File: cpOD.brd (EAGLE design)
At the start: 49.5 x 27.9 mm, 29 parts, among them IC1 LM358D, Q1 2N7002

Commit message: 2.0B-WIP
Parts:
- added R11: 10K, SPCoast:PT-10S
- added R12: 10K, SPCoast:TC33X
- C2: value 1uF -> 1.0uF
- R1: value 2.2M -> 2M2
- R10: value 10k -> 3K3
- R2, R3, R6: value 10k -> 10K
- R7: value 3.3k -> 1M
- R8: value 1M -> 10K; device SPCoast:0603-RES -> SPCoast:ST-4
- R9: value 10k -> 10K; device SPCoast:TC33X -> SPCoast:0603-RES
- moved R8 8.75 mm to (43.4, 17.1), turned to 90 degrees
- moved R9 8.64 mm to (45.7, 13.3), turned to 180 degrees
- moved LED1 6.11 mm to (46.6, 7.87), turned to 90 degrees
- moved R10 4.58 mm to (45.7, 11.4)
- moved R7 2.03 mm to (35.6, 13.3)
- moved C1 1.90 mm to (15.2, 11.4)
- moved FID2 0.90 mm to (47.6, 1.91)
- moved FID1 0.64 mm to (1.91, 25.4)
- turned R4 to 0 degrees
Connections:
- net DETECTED: now also R10.2, R7.1; no longer R7.2, R8.1
- net GND: now also R11.3, R12.2, R8.2; no longer R9.2
- net N$11: now also R10.1; no longer R7.1
- net SENS+: now also R11.1, R12.1, R8.1; no longer R10.1
- net SENSITIVITY: now also R11.2, R12.3, R7.2, R8.3; no longer R8.2, R9.3
- net V+: now also R9.2; no longer R10.2
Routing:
- net N$11: track 12.1 -> 2.81 mm, vias 2 -> 0
- net SENSITIVITY: track 30.9 -> 24.9 mm
- net DETECTED: track 36.0 -> 41.9 mm, vias 3 -> 4
- net !VOUT: track 39.9 -> 36.9 mm, vias 4 -> 3
- net INPUT-A: track 42.1 -> 41.3 mm
- net SENS+: track 5.15 -> 5.80 mm
- net GND: track 16.8 -> 16.9 mm, vias 3 -> 4
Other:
- board text added: "72p"
- board text added: "Engineering Test Sample 2"
- board text added: "KL2"
- board text added: "KL3"
- board text removed: "C1"
- board text removed: "C2"
- board text removed: "C3"
- board text removed: "C4"
- board text removed: "D1"
- board text removed: "D2"
- board text removed: "D3"
- board text removed: "D4"
- board text removed: "Engineering Test Sample"
- board text removed: "FID1"
- board text removed: "FID2"
- board text removed: "IC1"
- board text removed: "J1"
- board text removed: "LED1"
- board text removed: "Q1"
- board text removed: "R1"
- board text removed: "R10"
- board text removed: "R2"
- board text removed: "R3"
- board text removed: "R4"
- board text removed: "R5"
- board text removed: "R6"
- board text removed: "R7"
- board text removed: "R8"
- board text removed: "R9"

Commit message: Version 1.1
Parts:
- C1: value 0.1uF -> 1.0uF
- C2: value 1.0uF -> 0.01uF
- C3: value 0.01uF -> 0.1uF
- D2: value BAT54A -> BAT54C
- D3: value BAT54C -> BAT54A
- J1: device SPCoast:KK-156-5 -> SPCoast:1X05
- J2: device SPCoast:1X05 -> SPCoast:KK-156-5
- R10: value 3K3 -> 2k2
- R7: value 1M -> 10K
- R8: value 10K -> 1M; device SPCoast:ST-4 -> SPCoast:0603-RES
- R9: device SPCoast:0603-RES -> SPCoast:ST-4
- moved C2 11.0 mm to (26.0, 5.33), turned to 0 degrees
- moved J2 9.84 mm to (7.75, 17.8)
- moved J1 9.76 mm to (1.52, 10.2)
- moved R8 9.55 mm to (36.2, 10.9), turned to 180 degrees
- moved C3 6.66 mm to (31.1, 9.14)
- moved C4 6.13 mm to (31.1, 3.43), turned to 180 degrees
- moved R7 5.25 mm to (36.2, 18.5)
- moved R10 3.86 mm to (45.1, 7.62), turned to 270 degrees
- moved R9 2.84 mm to (44.5, 15.9), turned to 270 degrees
- moved C1 2.37 mm to (15.9, 9.14)
- moved R12 1.80 mm to (44.6, 15.9), turned to 270 degrees
- moved Q1 1.65 mm to (16.0, 5.97)
- moved R11 1.28 mm to (43.6, 15.9), turned to 270 degrees
- moved R3 0.74 mm to (26.0, 11.0)
- moved R4 0.74 mm to (26.0, 9.14)
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- renumbered U$5 to U$1, U$6 to U$2
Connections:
- net !VOUT: now also J1.3, J2.5; no longer J1.5, J2.3
- net DCC-A: now also J2.2; no longer J1.2
- net DCC-B: now also J2.4; no longer J1.4
- net DETECTED: now also R8.1; no longer R7.1
- net GND: now also C3.2, R9.2; no longer C2.2, R8.2
- net INPUT-A: now also D2.1, D3.2, J1.4; no longer D2.2, D3.1, J2.4
- net INPUT-B: now also D2.2, D3.1, J1.5; no longer D2.1, D3.2, J2.5
- net OCCUPIED: now also C1.1; no longer C2.1
- net SENS+: now also R7.1; no longer R8.1
- net SENSITIVITY: now also R8.2, R9.3; no longer R7.2, R8.3
- net STAGE1+: now also C3.1; no longer C4.1
- net STAGE1-: now also C2.1; no longer C3.1
- net TRIGGERED: now also C2.2; no longer C3.2
- net V+: now also C4.1, J1.2, J2.3, R7.2; no longer C1.1, J1.3, J2.2, R9.2
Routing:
- net INPUT-B: track 36.6 -> 43.6 mm
- net SENSITIVITY: track 24.9 -> 29.7 mm, vias 4 -> 3
- net INPUT-A: track 41.3 -> 37.6 mm
- net SENS+: track 5.80 -> 9.40 mm
- net DETECTED: track 41.9 -> 39.4 mm
- net INPUT-NEGATIVE: track 21.6 -> 20.2 mm
- net !VOUT: track 36.9 -> 37.9 mm, vias 3 -> 1
- net N$11: track 2.81 -> 1.97 mm
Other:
- board text added: "Test Sample 2"
- board text removed: "Engineering Test Sample 2"

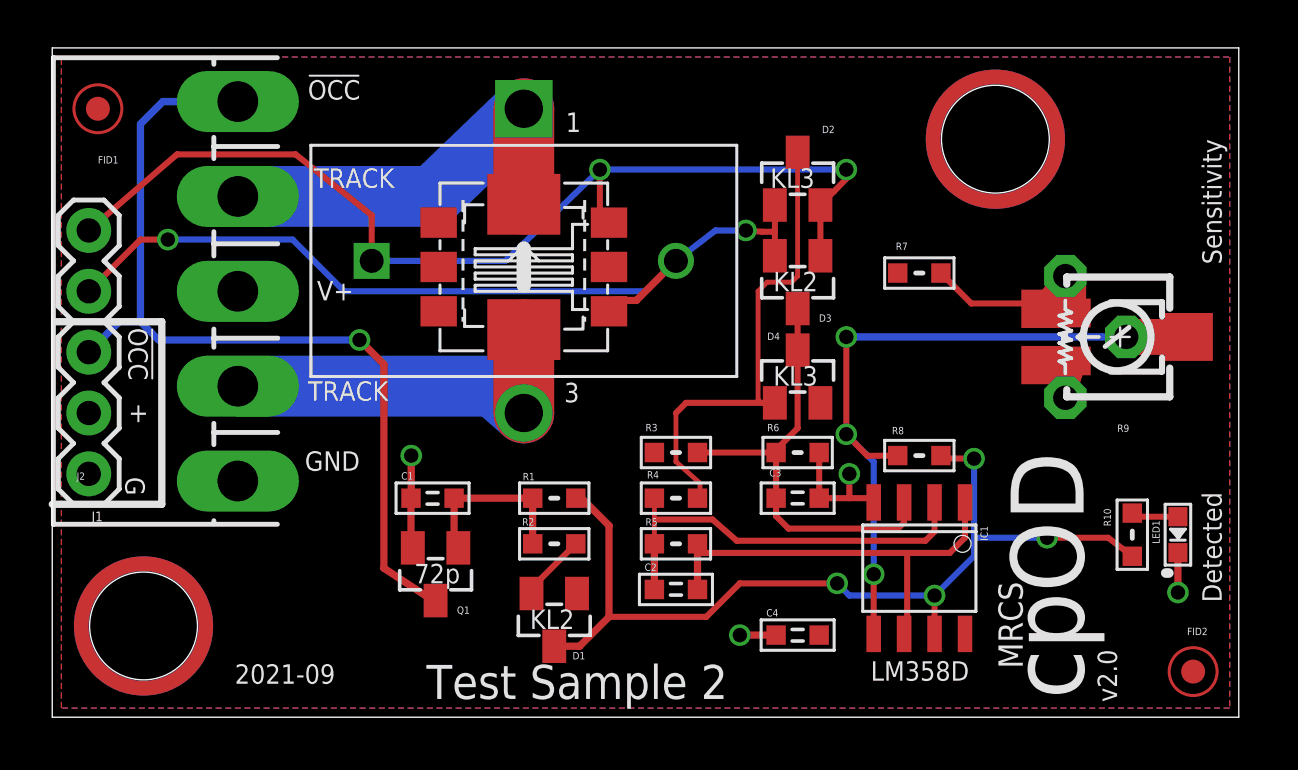
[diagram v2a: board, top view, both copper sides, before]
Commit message: LED1 shorted, D2/3 reversed
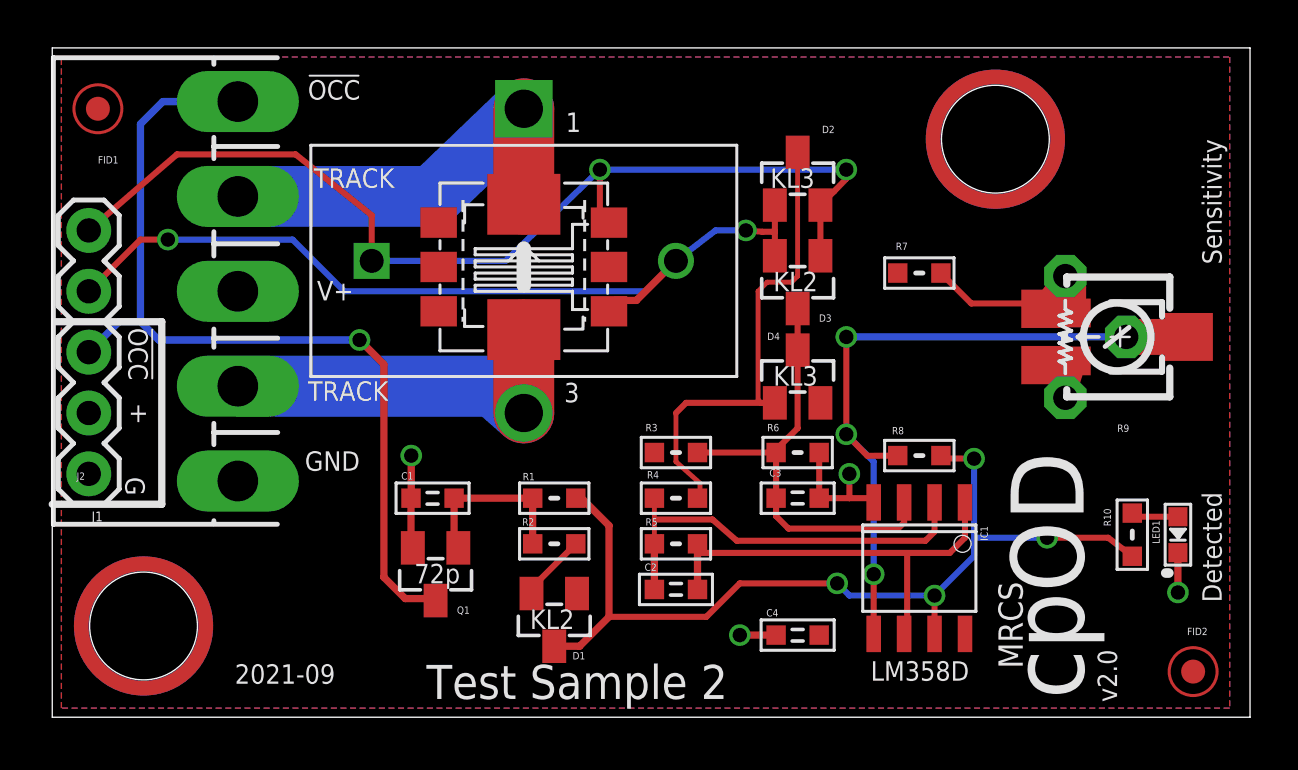
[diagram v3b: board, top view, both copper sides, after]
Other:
- board size 49.5 x 27.9 mm -> 50 x 27.9 mm
- board text added: "C1"
- board text added: "C2"
- board text added: "C3"
- board text added: "C4"
- board text added: "D1"
- board text added: "D2"
- board text added: "D3"
- board text added: "D4"
- board text added: "FID1"
- board text added: "FID2"
- board text added: "IC1"
- board text added: "J1"
- board text added: "LED1"
- board text added: "Q1"
- board text added: "R1"
- board text added: "R10"
- board text added: "R2"
- board text added: "R3"
- board text added: "R4"
- board text added: "R5"
- board text added: "R6"
- board text added: "R7"
- board text added: "R8"
- board text added: "R9"
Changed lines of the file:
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@@
 <setting verticaltext="up"/>
 </settings>
-<grid distance="50" unitdist="mil" unit="mil" style="dots" multiple="2" display="yes" altdistance="5" altunitdist="mil" altunit="mil"/>
+<grid distance="10" unitdist="mm" unit="mm" style="lines" multiple="5" display="yes" altdistance="1" altunitdist="mm" altunit="mm"/>
 <layers>
-<layer number="1" name="Top" color="4" fill="1" visible="no" active="yes"/>
-<layer number="16" name="Bottom" color="2" fill="1" visible="no" active="yes"/>
+<layer number="1" name="Top" color="4" fill="1" visible="yes" active="yes"/>
+<layer number="16" name="Bottom" color="2" fill="1" visible="yes" active="yes"/>
 <layer number="17" name="Pads" color="2" fill="1" visible="yes" active="yes"/>
 <layer number="18" name="Vias" color="1" fill="1" visible="yes" active="yes"/>
-<layer number="19" name="Unrouted" color="6" fill="1" visible="no" active="yes"/>
+<layer number="19" name="Unrouted" color="6" fill="1" visible="yes" active="yes"/>
 <layer number="20" name="Dimension" color="15" fill="1" visible="yes" active="yes"/>
-<layer number="21" name="tPlace" color="22" fill="1" visible="no" active="yes"/>
-<layer number="22" name="bPlace" color="22" fill="1" visible="yes" active="yes"/>
-<layer number="23" name="tOrigins" color="30" fill="1" visible="no" active="yes"/>
+<layer number="21" name="tPlace" color="22" fill="1" visible="yes" active="yes"/>
+<layer number="22" name="bPlace" color="22" fill="1" visible="no" active="yes"/>
+<layer number="23" name="tOrigins" color="30" fill="1" visible="yes" active="yes"/>
 <layer number="24" name="bOrigins" color="15" fill="1" visible="no" active="yes"/>
-<layer number="25" name="tNames" color="36" fill="1" visible="no" active="yes"/>
+<layer number="25" name="tNames" color="36" fill="1" visible="yes" active="yes"/>
 <layer number="26" name="bNames" color="34" fill="1" visible="no" active="yes"/>
-<layer number="27" name="tValues" color="22" fill="1" visible="no" active="yes"/>
-<layer number="28" name="bValues" color="7" fill="1" visible="yes" active="yes"/>
+<layer number="27" name="tValues" color="22" fill="1" visible="yes" active="yes"/>
+<layer number="28" name="bValues" color="7" fill="1" visible="no" active="yes"/>
 <layer number="29" name="tStop" color="5" fill="1" visible="no" active="yes"/>
 <layer number="30" name="bStop" color="7" fill="6" visible="no" active="yes"/>
@@
 <layer number="42" name="bRestrict" color="3" fill="10" visible="no" active="yes"/>
 <layer number="43" name="vRestrict" color="2" fill="10" visible="no" active="yes"/>
-<layer number="44" name="Drills" color="2" fill="1" visible="no" active="yes"/>
-<layer number="45" name="Holes" color="35" fill="1" visible="no" active="yes"/>
-<layer number="46" name="Milling" color="11" fill="1" visible="no" active="yes"/>
-<layer number="47" name="Measures" color="21" fill="1" visible="no" active="yes"/>
-<layer number="48" name="Document" color="49" fill="1" visible="no" active="yes"/>
-<layer number="49" name="Reference" color="7" fill="1" visible="no" active="yes"/>
+<layer number="44" name="Drills" color="2" fill="1" visible="yes" active="yes"/>
+<layer number="45" name="Holes" color="35" fill="1" visible="yes" active="yes"/>
+<layer number="46" name="Milling" color="11" fill="1" visible="yes" active="yes"/>
+<layer number="47" name="Measures" color="21" fill="1" visible="yes" active="yes"/>
+<layer number="48" name="Document" color="49" fill="1" visible="yes" active="yes"/>
+<layer number="49" name="Reference" color="7" fill="1" visible="yes" active="yes"/>
 <layer number="50" name="dxf" color="7" fill="1" visible="no" active="yes"/>
-<layer number="51" name="tDocu" color="24" fill="1" visible="no" active="yes"/>
-<layer number="52" name="bDocu" color="7" fill="1" visible="yes" active="yes"/>
+<layer number="51" name="tDocu" color="24" fill="1" visible="yes" active="yes"/>
+<layer number="52" name="bDocu" color="7" fill="1" visible="no" active="yes"/>
 <layer number="90" name="Modules" color="5" fill="1" visible="no" active="no"/>
 <layer number="91" name="Nets" color="2" fill="1" visible="no" active="no"/>
@@
 <layer number="59" name="tCarbon" color="7" fill="1" visible="no" active="no"/>
 <layer number="60" name="bCarbon" color="7" fill="1" visible="no" active="no"/>
-<layer number="125" name="_tNames" color="14" fill="1" visible="no" active="yes"/>
+<layer number="125" name="_tNames" color="14" fill="1" visible="yes" active="yes"/>
 </layers>
 <board>
@@
 <text x="7.62" y="1.397" size="0.8128" layer="21" font="vector" ratio="10">2021-09</text>
 <wire x1="0" y1="0" x2="0" y2="27.94" width="0" layer="20"/>
-<wire x1="0" y1="27.94" x2="49.53" y2="27.94" width="0" layer="20"/>
-<wire x1="49.53" y1="27.94" x2="49.53" y2="0" width="0" layer="20"/>
-<wire x1="49.53" y1="0" x2="0" y2="0" width="0" layer="20"/>
+<wire x1="0" y1="27.94" x2="50" y2="27.94" width="0" layer="20"/>
+<wire x1="50" y1="27.94" x2="50" y2="0" width="0" layer="20"/>
+<wire x1="50" y1="0" x2="0" y2="0" width="0" layer="20"/>
 <text x="34.163" y="1.524" size="0.8128" layer="21" font="vector">LM358D</text>
 <text x="39.624" y="7.239" size="3.81" layer="22" font="vector" ratio="15" rot="MR0">cpOD</text>
@@
 <text x="29.972" y="22.098" size="0.8128" layer="21" font="vector" ratio="10">KL3</text>
 <text x="30.099" y="13.843" size="0.8128" layer="21" font="vector" ratio="10">KL3</text>
+<text x="14.567003125" y="9.9210125" size="0.3048" layer="125" font="vector">C1</text>
+<text x="24.727003125" y="6.1110125" size="0.3048" layer="125" font="vector">C2</text>
+<text x="29.934003125" y="10.0480125" size="0.3048" layer="125" font="vector">C3</text>
+<text x="29.807003125" y="4.2060125" size="0.3048" layer="125" font="vector">C4</text>
+<text x="21.717" y="2.413" size="0.3048" layer="125" font="vector">D1</text>
+<text x="32.131" y="24.384" size="0.3048" layer="125" font="vector">D2</text>
+<text x="32.004" y="16.51" size="0.3048" layer="125" font="vector">D3</text>
+<text x="29.845" y="15.748" size="0.3048" layer="125" font="vector">D4</text>
+<text x="1.905" y="23.114" size="0.3048" layer="125" font="vector">FID1</text>
+<text x="47.371" y="3.429" size="0.3048" layer="125" font="vector">FID2</text>
+<text x="39.0525" y="7.366" size="0.3048" layer="125" font="vector" ratio="10" rot="R90">IC1</text>
+<text x="2.1082" y="8.5852" size="0.4064" layer="125" font="vector" rot="R180">J1</text>
+<text x="1.016" y="9.91199375" size="0.3048" layer="125" font="vector">J2</text>
+<text x="46.228" y="7.239" size="0.3048" layer="125" font="vector" rot="R90">LED1</text>
+<text x="16.891" y="4.318" size="0.3048" layer="125" font="vector">Q1</text>
+<text x="19.639" y="9.89299375" size="0.3048" layer="125" font="vector">R1</text>
+<text x="19.619009375" y="8.001" size="0.3048" layer="125" font="vector">R2</text>
+<text x="24.765" y="11.938" size="0.3048" layer="125" font="vector">R3</text>
+<text x="24.826009375" y="9.967009375" size="0.3048" layer="125" font="vector">R4</text>
+<text x="24.765" y="8.001" size="0.3048" layer="125" font="vector">R5</text>
+<text x="29.845" y="11.938" size="0.3048" layer="125" font="vector">R6</text>
+<text x="35.7124" y="19.812" size="0.3048" layer="125" font="vector" rot="R180">R7</text>
+<text x="35.052" y="11.811" size="0.3048" layer="125" font="vector">R8</text>
+<text x="44.958" y="12.2174" size="0.3048" layer="125" font="vector" ratio="10" rot="R180">R9</text>
+<text x="43.8912" y="8.7122" size="0.3048" layer="125" font="vector" rot="R270">R10</text>
 </plain>
 <attributes>
@@
 <contactref element="J2" pad="5"/>
 <via x="12.827" y="15.748" extent="1-16" drill="0.6"/>
-<wire x1="16.002" y1="5.334" x2="16.002" y2="4.869" width="0.3048" layer="1"/>
 <contactref element="J1" pad="3"/>
 <wire x1="1.524" y1="15.24" x2="2.794" y2="16.51" width="0.3048" layer="16"/>
@@
 <wire x1="12.827" y1="15.748" x2="4.445" y2="15.748" width="0.3048" layer="16"/>
 <wire x1="4.445" y1="15.748" x2="3.683" y2="16.51" width="0.3048" layer="16"/>
-<wire x1="13.843" y1="6.223" x2="13.843" y2="14.732" width="0.3048" layer="1"/>
+<wire x1="13.843" y1="5.842" x2="13.843" y2="14.732" width="0.3048" layer="1"/>
 <wire x1="13.843" y1="14.732" x2="12.827" y2="15.748" width="0.3048" layer="1"/>
 <wire x1="16.002" y1="4.869" x2="15.959" y2="4.826" width="0.3048" layer="1"/>
-<wire x1="15.959" y1="4.826" x2="13.843" y2="6.223" width="0.3048" layer="1"/>
+<wire x1="13.843" y1="5.842" x2="14.732" y2="4.953" width="0.3048" layer="1"/>
+<wire x1="14.732" y1="4.953" x2="15.918" y2="4.953" width="0.3048" layer="1"/>
+<wire x1="15.918" y1="4.953" x2="16.002" y2="4.869" width="0.3048" layer="1"/>
 </signal>
 <signal name="N$11">

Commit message: panelized
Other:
- board text added: "2021-10"
- board text removed: "2021-09"
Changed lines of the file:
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@@
 <setting verticaltext="up"/>
 </settings>
-<grid distance="10" unitdist="mm" unit="mm" style="lines" multiple="5" display="yes" altdistance="1" altunitdist="mm" altunit="mm"/>
+<grid distance="50" unitdist="mil" unit="mil" style="dots" multiple="2" display="yes" altdistance="25" altunitdist="mil" altunit="mil"/>
 <layers>
 <layer number="1" name="Top" color="4" fill="1" visible="yes" active="yes"/>
@@
 <text x="48.006" y="24.13" size="0.8128" layer="21" font="vector" rot="R270">Sensitivity</text>
 <text x="9.0678" y="3.6449" size="1.016" layer="22" font="vector" ratio="10" rot="MR180">John Plocher</text>
-<text x="7.62" y="1.397" size="0.8128" layer="21" font="vector" ratio="10">2021-09</text>
+<text x="7.62" y="1.397" size="0.8128" layer="21" font="vector" ratio="10">2021-10</text>
 <wire x1="0" y1="0" x2="0" y2="27.94" width="0" layer="20"/>
 <wire x1="0" y1="27.94" x2="50" y2="27.94" width="0" layer="20"/>

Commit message: Version 2.0
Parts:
- removed FID1, FID2: FIDUCIAL, SPCoast:FIDUCIAL_1MM
- turned IC1 to 180 degrees
- turned R12 to 180 degrees
- turned R9 to 180 degrees
- turned X2 to 0 degrees
- renumbered U$1 to MH1, U$2 to MH2
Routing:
- net DETECTED: track 39.4 -> 41.2 mm
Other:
- board text added: "DCC"
- board text added: "DCC / Common"
- board text removed: "FID1"
- board text removed: "FID2"
- board text removed: "Test Sample 2"
